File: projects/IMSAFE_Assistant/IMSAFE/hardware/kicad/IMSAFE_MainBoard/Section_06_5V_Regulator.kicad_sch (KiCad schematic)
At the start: 0 parts

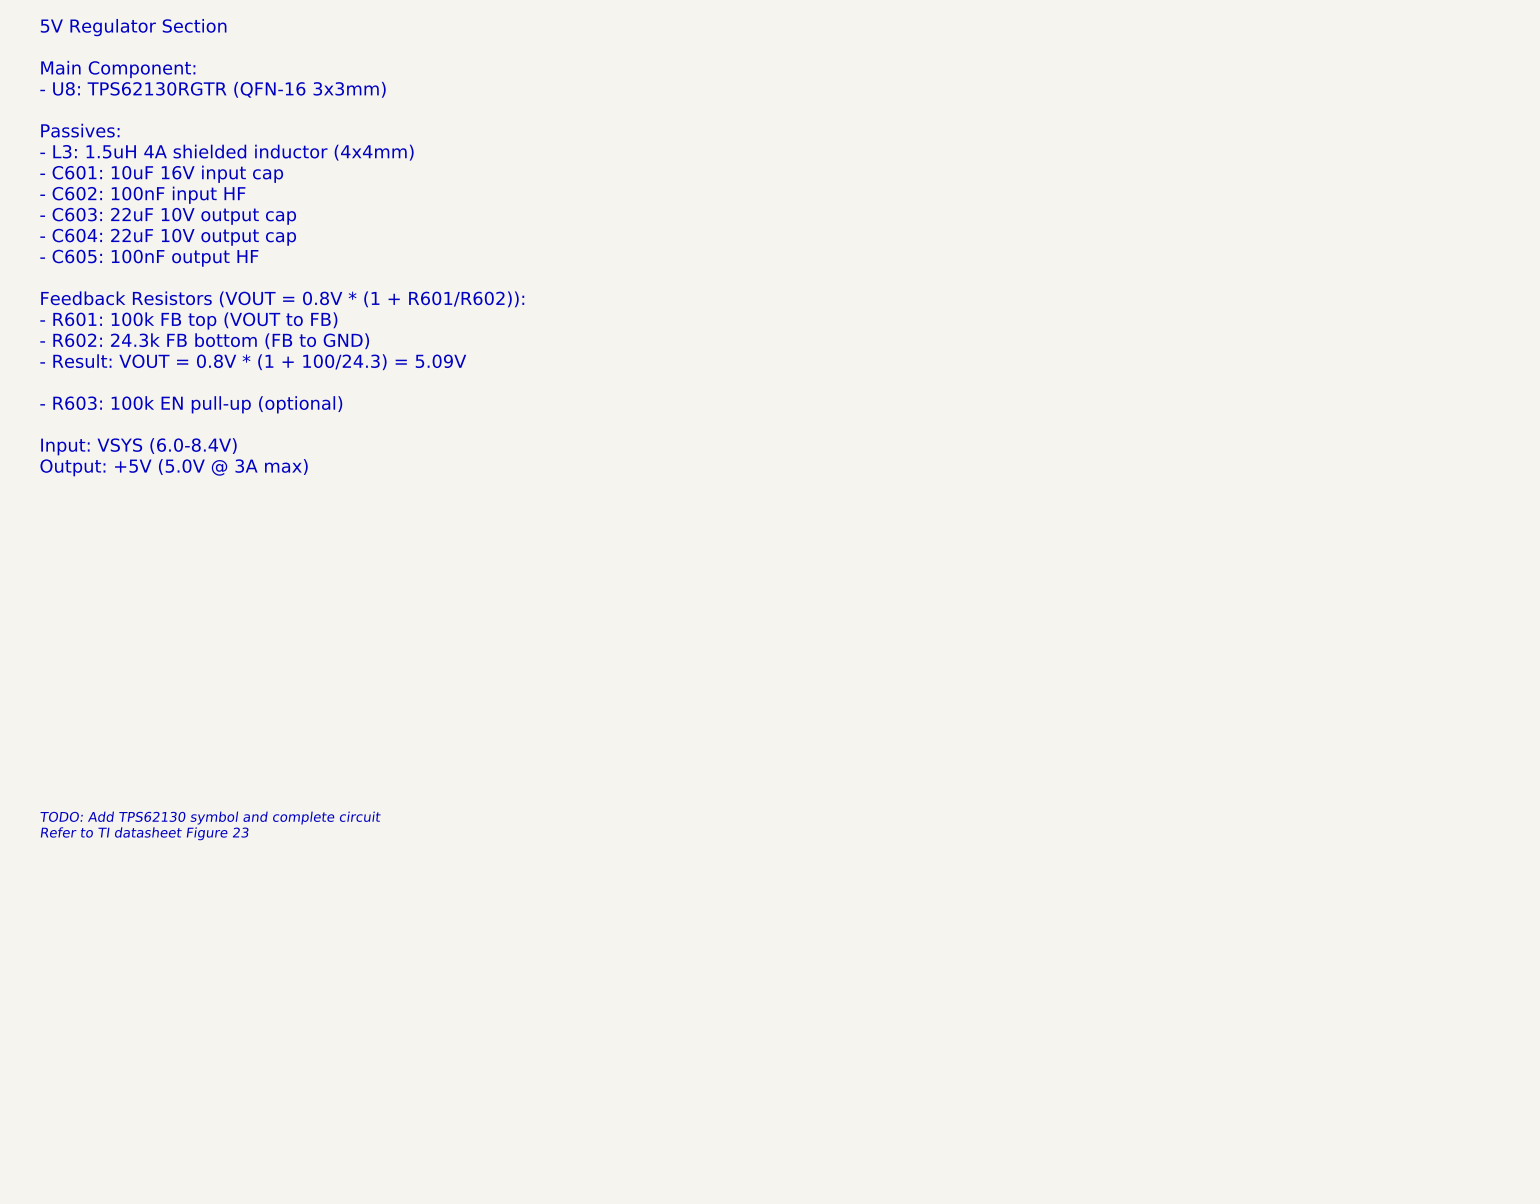
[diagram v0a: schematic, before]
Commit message: Add Sections 05-06: 3.3V and 5V buck regulators
Section 05 - TPS62133 (3.3V Fixed):
- 3A synchronous buck converter
- Input: VSYS (6-8.4V), Output: 3.3V
- Components: L2 (1.5µH), C501-C505, R501 (EN pull-up)
- Powers MCU and digital peripherals

Section 06 - TPS62130 (5V Adjustable):
- 3A synchronous buck converter with FB divider
- Input: VSYS, Output: 5.09V (R601=100k, R602=24.3k)
- Components: L3 (1.5µH), C601-C605, R601-R603
- Powers WS2812B LEDs, display, buzzer

Co-Authored-By: Claude Opus 4.5 <noreply@anthropic.com>
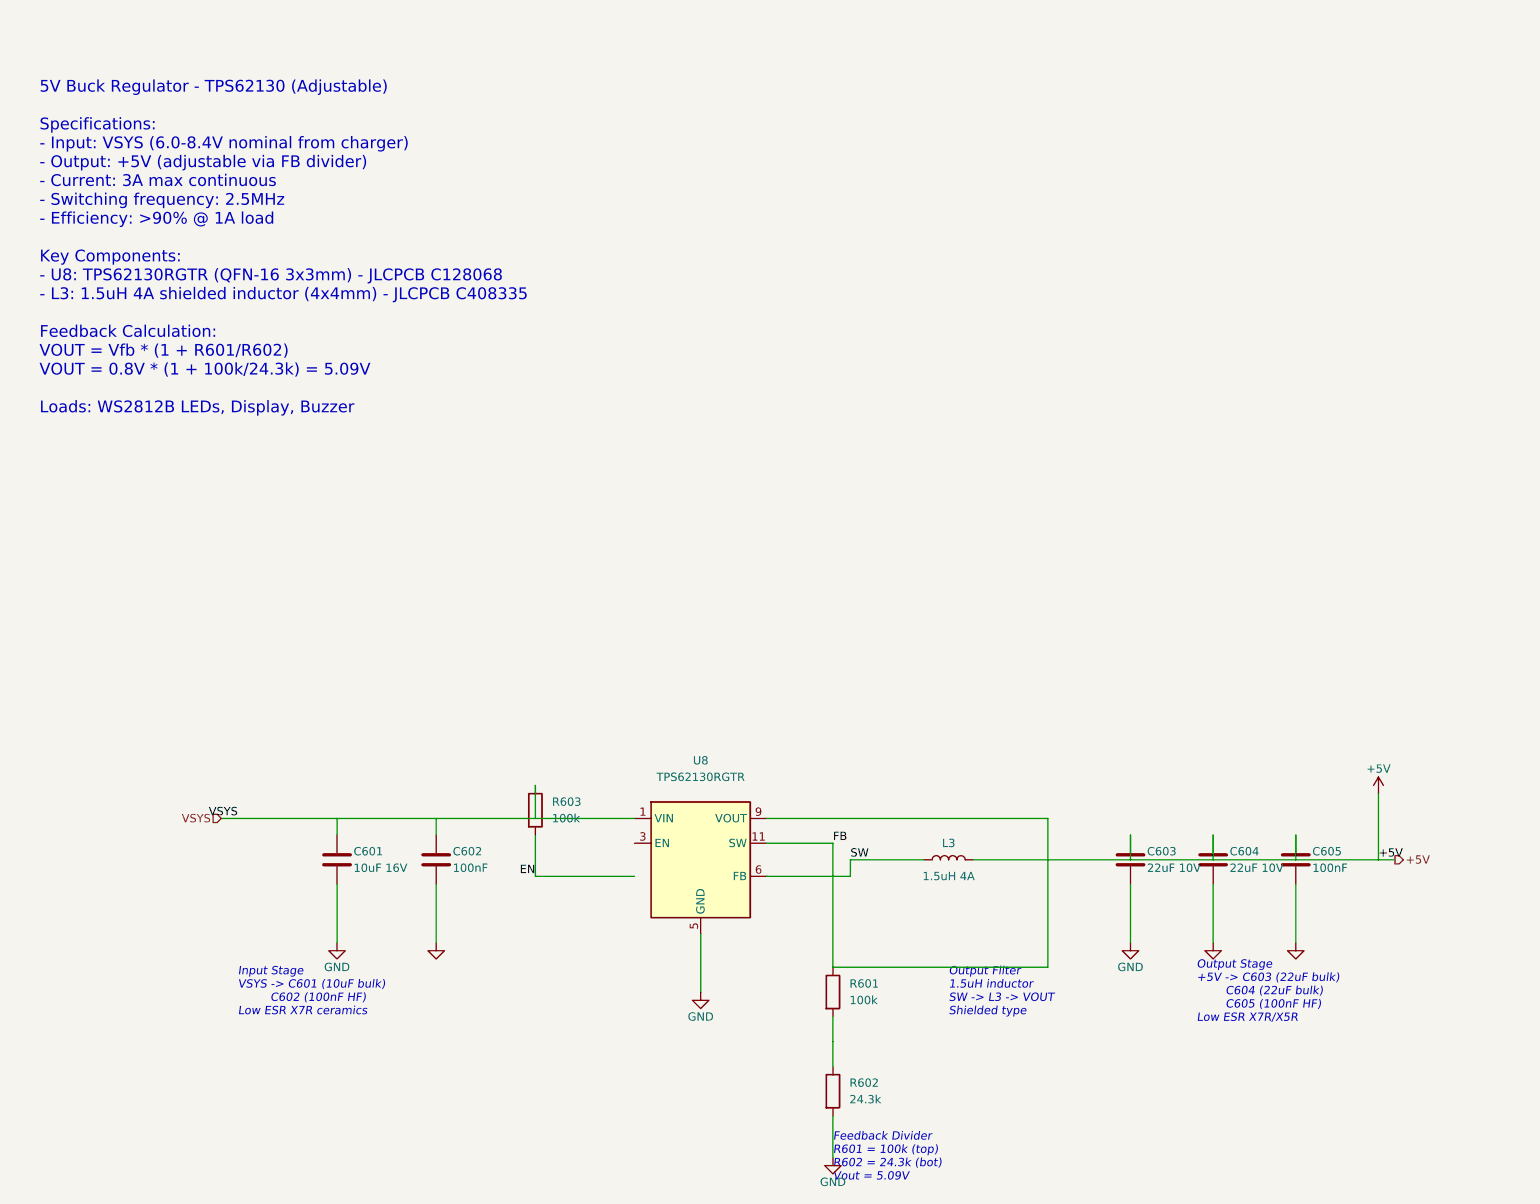
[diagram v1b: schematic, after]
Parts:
- added C601: 10uF 16V, Capacitor_SMD:C_0805_2012Metric, symbol Device:C
- added C602, C605: 100nF, Capacitor_SMD:C_0603_1608Metric, symbol Device:C
- added C603, C604: 22uF 10V, Capacitor_SMD:C_0805_2012Metric, symbol Device:C
- added L3: 1.5uH 4A, Inductor_SMD:L_4x4mm_H2.5mm, symbol Device:L
- added R601, R603: 100k, Resistor_SMD:R_0603_1608Metric, symbol Device:R
- added R602: 24.3k, Resistor_SMD:R_0603_1608Metric, symbol Device:R
- added U8: TPS62130RGTR, Package_DFN_QFN:QFN-16-1EP_3x3mm_P0.5mm_EP1.8x1.8mm, symbol Regulator:TPS62130RGTR
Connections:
- new net: R601.2, R602.1
- new net +5V: C603.1, C604.1, C605.1, L3.2, R601.1, U8.11 (SW), U8.9 (VOUT)
- new net EN: R603.2
- new net GND: C601.2, C602.2, C603.2, C604.2, C605.2, R602.2, U8.5 (GND)
- new net SW: L3.1, U8.6 (FB)
- new net VSYS: C601.1, C602.1, R603.1, U8.1 (VIN)
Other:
- note added: "5V Buck Regulator - TPS62130 (Adjustable) Specifications: - Input: VSYS (6.0-8.4V nominal from charger) - Output: +5V (adjustable via FB divider) - Current: 3A max continuous - Switching frequency: 2.5MHz - Efficiency: >90% @ 1A load Key Components: - U8: TPS62130RGTR (QFN-16 3x3mm) - JLCPCB C128068 - L3: 1.5uH 4A shielded inductor (4x4mm) - JLCPCB C408335 Feedback Calculation: VOUT = Vfb * (1 + 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"
- note added: "Feedback Divider R601 = 100k (top) R602 = 24.3k (bot) Vout = 5.09V"
- note added: "Input Stage VSYS -> C601 (10uF bulk) C602 (100nF HF) Low ESR X7R ceramics"
- note added: "Output Filter 1.5uH inductor SW -> L3 -> VOUT Shielded type"
- note added: "Output Stage +5V -> C603 (22uF bulk) C604 (22uF bulk) C605 (100nF HF) Low ESR X7R/X5R"
- note removed: "5V Regulator Section Main Component: - U8: TPS62130RGTR (QFN-16 3x3mm) Passives: - L3: 1.5uH 4A shielded inductor (4x4mm) - C601: 10uF 16V input cap - C602: 100nF input HF - C603: 22uF 10V output cap - C604: 22uF 10V output cap - C605: 100nF output HF Feedback Resistors (VOUT = 0.8V * (1 + R601/R602)): - R601: 100k FB top (VOUT to FB) - R602: 24.3k FB bottom (FB to GND) - Result: VOUT = 0.8V * (1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"
- note removed: "TODO: Add TPS62130 symbol and complete circuit Refer to TI datasheet Figure 23"

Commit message: Fix Section 06 FB divider for correct 5V output
- Change R602 from 24.3k to 19.1k (JLCPCB C25947)
- Corrects output voltage from 4.09V to 5.03V
- Update schematic text annotations with correct calculations
- Update design-rationale.md to reflect the fix
- Add PWR_FLAG symbols to Sections 04, 05, 06 for ERC compliance

Co-Authored-By: Claude Opus 4.5 <noreply@anthropic.com>
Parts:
- R602: value 24.3k -> 19.1k; JLCPCB C25959 -> C25947
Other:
- note added: "Feedback Divider R601 = 100k (top) R602 = 19.1k (bot) Vout = 5.03V"
- note removed: "Feedback Divider R601 = 100k (top) R602 = 24.3k (bot) Vout = 5.09V"
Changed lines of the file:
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@@
 		(comment 2 "5.0V @ 3A for LEDs, display, buzzer")
 	)
-	(text "5V Buck Regulator - TPS62130 (Adjustable)\n\nSpecifications:\n- Input: VSYS (6.0-8.4V nominal from charger)\n- Output: +5V (adjustable via FB divider)\n- Current: 3A max continuous\n- Switching frequency: 2.5MHz\n- Efficiency: >90% @ 1A load\n\nKey Components:\n- U8: TPS62130RGTR (QFN-16 3x3mm) - JLCPCB C128068\n- L3: 1.5uH 4A shielded inductor (4x4mm) - JLCPCB C408335\n\nFeedback Calculation:\nVOUT = Vfb * (1 + R601/R602)\nVOUT = 0.8V * (1 + 100k/24.3k) = 5.09V\n\nLoads: WS2812B LEDs, Display, Buzzer"
+	(text "5V Buck Regulator - TPS62130 (Adjustable)\n\nSpecifications:\n- Input: VSYS (6.0-8.4V nominal from charger)\n- Output: +5V (adjustable via FB divider)\n- Current: 3A max continuous\n- Switching frequency: 2.5MHz\n- Efficiency: >90% @ 1A load\n\nKey Components:\n- U8: TPS62130RGTR (QFN-16 3x3mm) - JLCPCB C128068\n- L3: 1.5uH 4A shielded inductor (4x4mm) - JLCPCB C408335\n\nFeedback Calculation:\nVOUT = Vfb * (1 + R601/R602)\nVOUT = 0.8V * (1 + 100k/19.1k) = 5.03V\n\nLoads: WS2812B LEDs, Display, Buzzer"
 		(exclude_from_sim no)
 		(at 25.4 25.4 0)
@@
 		(uuid "text-inductor-001")
 	)
-	(text "Feedback Divider\nR601 = 100k (top)\nR602 = 24.3k (bot)\nVout = 5.09V"
+	(text "Feedback Divider\nR601 = 100k (top)\nR602 = 19.1k (bot)\nVout = 5.03V"
 		(exclude_from_sim no)
 		(at 147.32 165.1 0)
@@
 		(uuid "r602-uuid")
 		(property "Reference" "R602" (at 149.86 153.67 0) (effects (font (size 1.27 1.27)) (justify left)))
-		(property "Value" "24.3k" (at 149.86 156.21 0) (effects (font (size 1.27 1.27)) (justify left)))
+		(property "Value" "19.1k" (at 149.86 156.21 0) (effects (font (size 1.27 1.27)) (justify left)))
 		(property "Footprint" "Resistor_SMD:R_0603_1608Metric" (at 145.542 154.94 90) (effects (font (size 1.27 1.27)) hide))
 		(property "Datasheet" "~" (at 147.32 154.94 0) (effects (font (size 1.27 1.27)) hide))
-		(property "JLCPCB" "C25959" (at 147.32 154.94 0) (effects (font (size 1.27 1.27)) hide))
+		(property "JLCPCB" "C25947" (at 147.32 154.94 0) (effects (font (size 1.27 1.27)) hide))
 		(pin "1" (uuid "r602-p1")) (pin "2" (uuid "r602-p2"))
 		(instances (project "IMSAFE_MainBoard" (path "/sec06-0001-0002-0003-000000000001" (reference "R602") (unit 1))))
@@
 	(wire (pts (xy 53.34 113.03) (xy 55.88 113.03)) (stroke (width 0) (type default)) (uuid "w-hl-vsys"))
 	(wire (pts (xy 231.14 119.38) (xy 233.68 119.38)) (stroke (width 0) (type default)) (uuid "w-hl-5v"))
+	(symbol (lib_id "power:PWR_FLAG") (at 63.5 113.03 0) (unit 1)
+		(exclude_from_sim no) (in_bom yes) (on_board yes) (dnp no)
+		(uuid "pwr-flag-vsys-06")
+		(property "Reference" "#FLG0601" (at 63.5 111.125 0) (effects (font (size 1.27 1.27)) hide))
+		(property "Value" "PWR_FLAG" (at 63.5 109.22 0) (effects (font (size 1.27 1.27))))
+		(property "Footprint" "" (at 63.5 113.03 0) (effects (font (size 1.27 1.27)) hide))
+		(property "Datasheet" "~" (at 63.5 113.03 0) (effects (font (size 1.27 1.27)) hide))
+		(pin "1" (uuid "pwr-flag-vsys-06-p1"))
+		(instances (project "IMSAFE_MainBoard" (path "/sec06-0001-0002-0003-000000000001" (reference "#FLG0601") (unit 1))))
+	)
 	(sheet_instances (path "/" (page "1")))
 )

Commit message: Fix ERC errors across multiple schematic sections
- Section_04_BMS: Add VSYS hierarchical label for root schematic connection
- Section_05/06 Regulators: Add PWR_FLAG wire and junction to VSYS net
- Section_07_Barometric: Connect BMP390 SCK pin to GND for I2C mode
- Section_14_IO_Expander: Add no-connect symbols for unused MCP23017 GPIO pins
- Update design-rationale.md with ERC remediation status

Co-Authored-By: Claude Opus 4.5 <noreply@anthropic.com>
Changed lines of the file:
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@@
 	(wire (pts (xy 53.34 113.03) (xy 55.88 113.03)) (stroke (width 0) (type default)) (uuid "w-hl-vsys"))
 	(wire (pts (xy 231.14 119.38) (xy 233.68 119.38)) (stroke (width 0) (type default)) (uuid "w-hl-5v"))
+	(wire (pts (xy 55.88 113.03) (xy 63.5 113.03)) (stroke (width 0) (type default)) (uuid "w-pwr-flag-vsys-06"))
+	(junction (at 55.88 113.03) (diameter 0) (color 0 0 0 0) (uuid "junction-vsys-main-06"))
 	(symbol (lib_id "power:PWR_FLAG") (at 63.5 113.03 0) (unit 1)
 		(exclude_from_sim no) (in_bom yes) (on_board yes) (dnp no)

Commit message: Fix additional ERC errors in regulator and IO expander sections
- Section_05/06: Remove redundant PWR_FLAG on VSYS (BMS provides power_output)
- Section_14: Correct MCP23017 NC symbol positions to match actual pin coordinates

ERC reduction: 412 → 390 violations (22 fewer)
- Errors: 150 → 129 (-21)
- Warnings: 262 → 261 (-1)

Co-Authored-By: Claude Opus 4.5 <noreply@anthropic.com>
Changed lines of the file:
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@@
 	(wire (pts (xy 53.34 113.03) (xy 55.88 113.03)) (stroke (width 0) (type default)) (uuid "w-hl-vsys"))
 	(wire (pts (xy 231.14 119.38) (xy 233.68 119.38)) (stroke (width 0) (type default)) (uuid "w-hl-5v"))
-	(wire (pts (xy 55.88 113.03) (xy 63.5 113.03)) (stroke (width 0) (type default)) (uuid "w-pwr-flag-vsys-06"))
-	(junction (at 55.88 113.03) (diameter 0) (color 0 0 0 0) (uuid "junction-vsys-main-06"))
-	(symbol (lib_id "power:PWR_FLAG") (at 63.5 113.03 0) (unit 1)
-		(exclude_from_sim no) (in_bom yes) (on_board yes) (dnp no)
-		(uuid "pwr-flag-vsys-06")
-		(property "Reference" "#FLG0601" (at 63.5 111.125 0) (effects (font (size 1.27 1.27)) hide))
-		(property "Value" "PWR_FLAG" (at 63.5 109.22 0) (effects (font (size 1.27 1.27))))
-		(property "Footprint" "" (at 63.5 113.03 0) (effects (font (size 1.27 1.27)) hide))
-		(property "Datasheet" "~" (at 63.5 113.03 0) (effects (font (size 1.27 1.27)) hide))
-		(pin "1" (uuid "pwr-flag-vsys-06-p1"))
-		(instances (project "IMSAFE_MainBoard" (path "/sec06-0001-0002-0003-000000000001" (reference "#FLG0601") (unit 1))))
-	)
 	(sheet_instances (path "/" (page "1")))
 )
